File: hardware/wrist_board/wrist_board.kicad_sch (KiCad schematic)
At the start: 0 parts

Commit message: Added hierarchical pages and 3v3 circuitry
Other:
- added sheet ESP and Comms (esp_and_comms.kicad_sch)
- added sheet power (power.kicad_sch)
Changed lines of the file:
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@@
 	(generator_version "9.0")
 	(paper "A4")
+	(sheet
+		(at 64.77 53.34)
+		(size 31.75 25.4)
+		(exclude_from_sim no)
+		(in_bom yes)
+		(on_board yes)
+		(dnp no)
+		(fields_autoplaced yes)
+		(stroke
+			(width 0.1524)
+			(type solid)
+		)
+		(fill
+			(color 0 0 0 0.0000)
+		)
+		(property "Sheetname" "power"
+			(at 64.77 52.6284 0)
+			(effects
+				(font
+					(size 1.27 1.27)
+				)
+				(justify left bottom)
+			)
+		)
+		(property "Sheetfile" "power.kicad_sch"
+			(at 64.77 79.3246 0)
+			(effects
+				(font
+					(size 1.27 1.27)
+				)
+				(justify left top)
+			)
+		)
+		(instances
+			(project "wrist_board"
+				(path "/530b8e3e-eee5-4922-ab86-607fb3fa4192"
+					(page "2")
+				)
+			)
+		)
+	)
+	(sheet
+		(at 101.6 53.34)
+		(size 35.56 25.4)
+		(exclude_from_sim no)
+		(in_bom yes)
+		(on_board yes)
+		(dnp no)
+		(fields_autoplaced yes)
+		(stroke
+			(width 0.1524)
+			(type solid)
+		)
+		(fill
+			(color 0 0 0 0.0000)
+		)
+		(property "Sheetname" "ESP and Comms"
+			(at 101.6 52.6284 0)
+			(effects
+				(font
+					(size 1.27 1.27)
+				)
+				(justify left bottom)
+			)
+		)
+		(property "Sheetfile" "esp_and_comms.kicad_sch"
+			(at 101.6 79.3246 0)
+			(effects
+				(font
+					(size 1.27 1.27)
+				)
+				(justify left top)
+			)
+		)
+		(instances
+			(project "wrist_board"
+				(path "/530b8e3e-eee5-4922-ab86-607fb3fa4192"
+					(page "3")
+				)
+			)
+		)
+	)
 	(sheet_instances
 		(path "/"

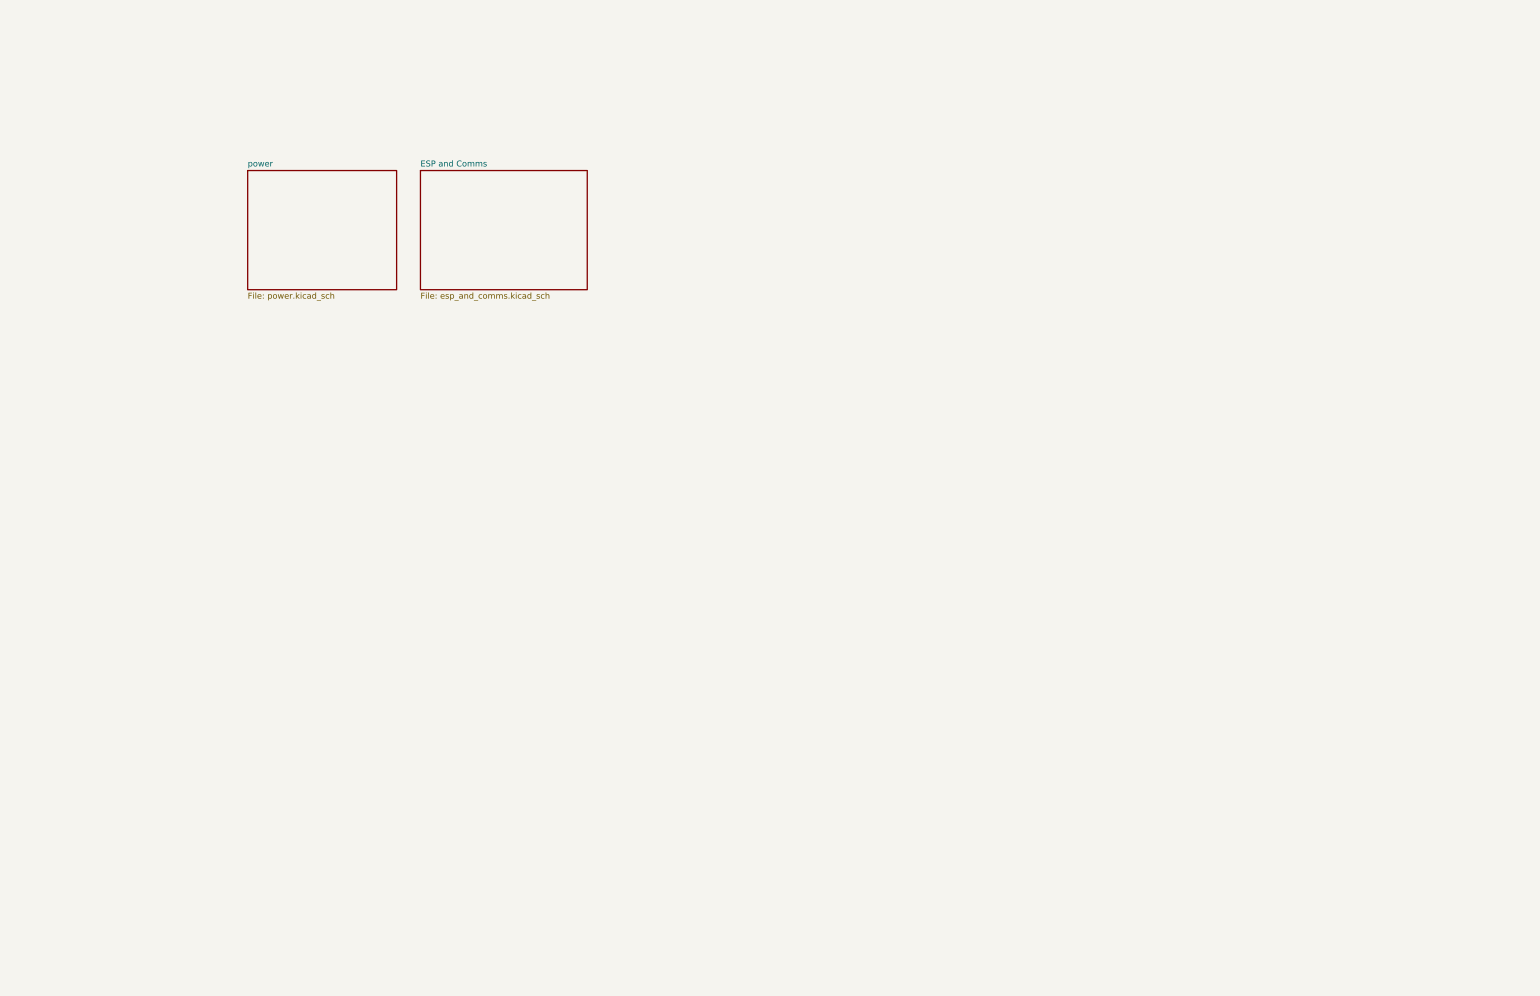
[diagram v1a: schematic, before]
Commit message: Schematics condensed into one, labels added
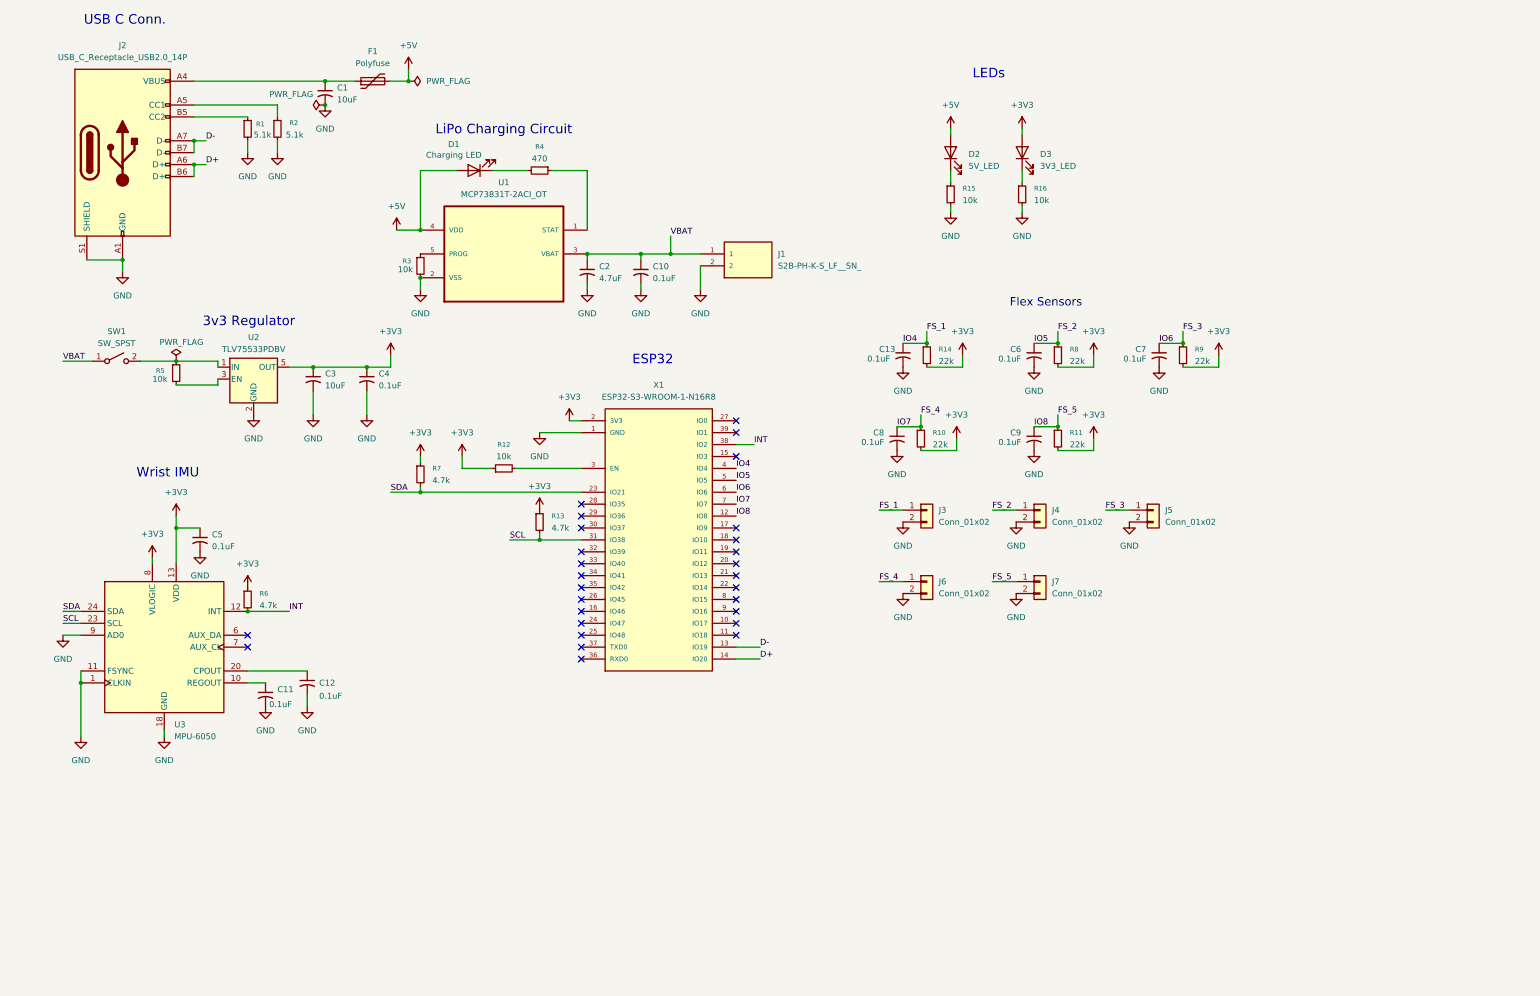
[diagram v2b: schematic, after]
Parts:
- added C1, C3: 10uF, Capacitor_SMD:C_0201_0603Metric, symbol Device:C_Small_US
- added C10, C11, C12, C13, C4, C5, C6, C7, C8, C9: 0.1uF, Capacitor_SMD:C_0402_1005Metric, symbol Device:C_Small_US
- added C2: 4.7uF, Capacitor_SMD:C_0201_0603Metric, symbol Device:C_Small_US
- added D1: Charging LED, LED_SMD:LED_0201_0603Metric, symbol Device:LED
- added D2: 5V_LED, LED_SMD:LED_0201_0603Metric, symbol Device:LED
- added D3: 3V3_LED, LED_SMD:LED_0201_0603Metric, symbol Device:LED
- added F1: Polyfuse, Fuse:Fuse_0805_2012Metric, symbol Device:Polyfuse
- added J1: S2B-PH-K-S_LF__SN_, S2B-PH-K-S_LF__SN_:JST_S2B-PH-K-S_LF__SN_, symbol S2B-PH-K-S_LF__SN_:S2B-PH-K-S_LF__SN_
- added J2: USB_C_Receptacle_USB2.0_14P, Connector_USB:USB_C_Receptacle_GCT_USB4105-xx-A_16P_TopMnt_Horizontal, symbol Connector:USB_C_Receptacle_USB2.0_14P
- added J3, J4, J5, J6, J7: Conn_01x02, Connector_PinHeader_2.54mm:PinHeader_1x02_P2.54mm_Vertical, symbol Connector_Generic:Conn_01x02
- added R1, R2: 5.1k, Resistor_SMD:R_0402_1005Metric, symbol Device:R_Small
- added R10, R11, R14, R8, R9: 22k, Resistor_SMD:R_0402_1005Metric, symbol Device:R_Small
- added R12, R5: 10k, Resistor_SMD:R_0402_1005Metric, symbol Device:R_Small
- added R13, R6, R7: 4.7k, Resistor_SMD:R_0402_1005Metric, symbol Device:R_Small
- added R15, R16: 10k, Resistor_SMD:R_0603_1608Metric, symbol Device:R_Small
- added R3: 10k, LED_SMD:LED_0402_1005Metric, symbol Device:R_Small
- added R4: 470, Resistor_SMD:R_0603_1608Metric, symbol Device:R_Small
- added SW1: SW_SPST, Button_Switch_THT:SW_DIP_SPSTx01_Slide_6.7x4.1mm_W7.62mm_P2.54mm_LowProfile, symbol Switch:SW_SPST
- added U1: MCP73831T-2ACI_OT, MCP73831T-2ACI_OT:SOT95P280X145-5N, symbol MCP73831T-2ACI_OT:MCP73831T-2ACI_OT
- added U2: TLV75533PDBV, Package_TO_SOT_SMD:SOT-23-5, symbol Regulator_Linear:TLV75533PDBV
- added U3: MPU-6050, Sensor_Motion:InvenSense_QFN-24_4x4mm_P0.5mm, symbol Sensor_Motion:MPU-6050
- added X1: ESP32-S3-WROOM-1-N16R8, ESP32-S3-WROOM-1-N16R8:ESP32S3WROOM1N8R2, symbol ESP32-S3-WROOM-1-N16R8:ESP32-S3-WROOM-1-N16R8
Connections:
- new net: D3.1 (K), R16.1
- new net: D1.1 (K), R4.2
- new net: C10.1, C2.1, J1.1, SW1.1 (A), U1.3 (VBAT)
- new net: R12.2, X1.3 (EN)
- new net: C1.1, F1.1, J2.A4 (VBUS), J2.A9 (VBUS), J2.B4 (VBUS), J2.B9 (VBUS)
- new net: C11.1, U3.10 (REGOUT)
- new net: C12.1, U3.20 (CPOUT)
- new net: D2.1 (K), R15.1
- new net: R5.1, SW1.2 (B), U2.1 (IN)
- new net: R4.1, U1.1 (STAT)
- new net: R3.1, U1.5 (PROG)
- new net: J2.B5 (CC2), R1.1
- new net: J2.A5 (CC1), R2.1
- new net: R5.2, U2.3 (EN)
- new net +3V3: C3.1, C4.1, C5.1, D3.2 (A), R10.2, R11.2, R12.1, R13.1, R14.2, R6.1, R7.1, R8.2, R9.2, U2.5 (OUT), U3.13 (VDD), U3.8 (VLOGIC), X1.2 (3V3)
- new net +5V: D1.2 (A), D2.2 (A), F1.2, U1.4 (VDD)
- new net D+: J2.A6 (D+), J2.B6 (D+), X1.14 (IO20)
- new net D-: J2.A7 (D-), J2.B7 (D-), X1.13 (IO19)
- new net FS_1: C13.1, J3.1 (Pin_1), R14.1, X1.4 (IO4)
- new net FS_2: C6.1, J4.1 (Pin_1), R8.1, X1.5 (IO5)
- new net FS_3: C7.1, J5.1 (Pin_1), R9.1, X1.6 (IO6)
- new net FS_4: C8.1, J6.1 (Pin_1), R10.1, X1.7 (IO7)
- new net FS_5: C9.1, J7.1 (Pin_1), R11.1, X1.12 (IO8)
- new net GND: C1.2, C10.2, C11.2, C12.2, C13.2, C2.2, C3.2, C4.2, C5.2, C6.2, C7.2, C8.2, C9.2, J1.2, J2.A1 (GND), J2.A12 (GND), J2.B1 (GND), J2.B12 (GND), J2.S1 (SHIELD), J3.2 (Pin_2), J4.2 (Pin_2), J5.2 (Pin_2), J6.2 (Pin_2), J7.2 (Pin_2), R1.2, R15.2, R16.2, R2.2, R3.2, U1.2 (VSS), U2.2 (GND), U3.1 (CLKIN), U3.11 (FSYNC), U3.18 (GND), U3.9 (AD0), X1.1 (GND), X1.40 (GND), X1.41 (GND), X1.42 (GND), X1.43 (GND), X1.44 (GND), X1.45 (GND), X1.46 (GND), X1.47 (GND), X1.48 (GND), X1.49 (GND)
- new net INT: R6.2, U3.12 (INT), X1.38 (IO2)
- new net SCL: R13.2, U3.23 (SCL), X1.31 (IO38)
- new net SDA: R7.2, U3.24 (SDA), X1.23 (IO21)
- no-connect marks 0 -> 28
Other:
- removed sheet ESP and Comms
- removed sheet power
- note added: "3v3 Regulator"
- note added: "ESP32"
- note added: "Flex Sensors"
- note added: "LEDs"
- note added: "LiPo Charging Circuit"
- note added: "USB C Conn."
- note added: "Wrist IMU"

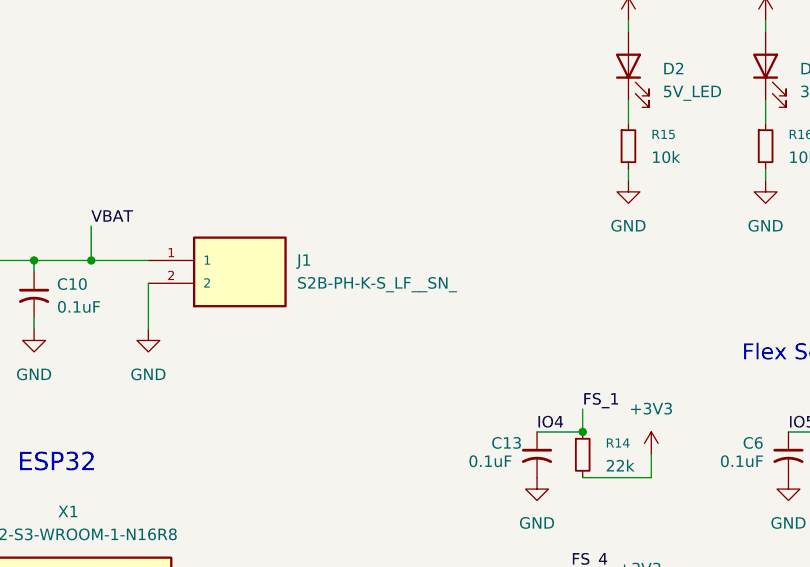
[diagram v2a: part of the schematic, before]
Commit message: New board orientation + USB/PWR routing
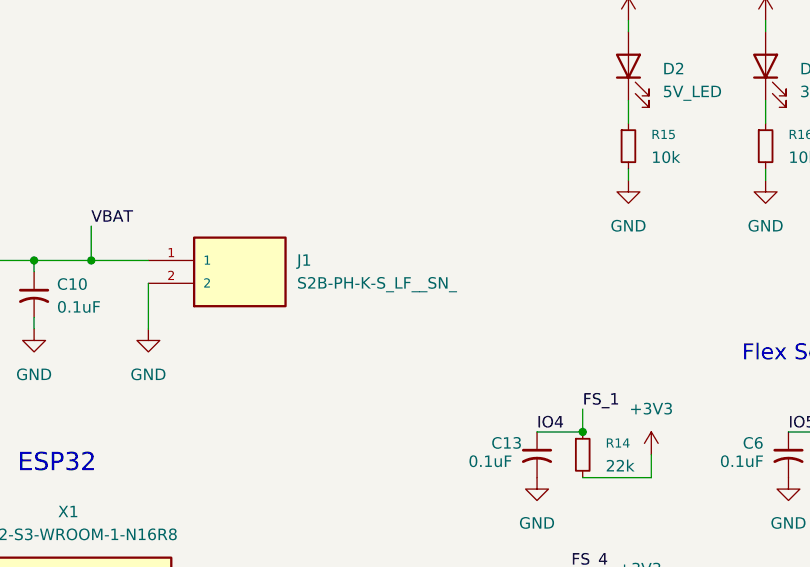
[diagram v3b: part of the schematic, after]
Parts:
- C1, C2, C3: footprint Capacitor_SMD:C_0201_0603Metric -> Capacitor_SMD:C_0805_2012Metric
- C10, C11, C12, C13, C4, C5, C6, C7, C8, C9: footprint Capacitor_SMD:C_0402_1005Metric -> Capacitor_SMD:C_0805_2012Metric
- D1, D2, D3: footprint LED_SMD:LED_0201_0603Metric -> LED_SMD:LED_0805_2012Metric
- R1, R10, R11, R12, R13, R14, R2, R5, R6, R7, R8, R9: footprint Resistor_SMD:R_0402_1005Metric -> Resistor_SMD:R_0805_2012Metric
- R15, R16, R4: footprint Resistor_SMD:R_0603_1608Metric -> Resistor_SMD:R_0805_2012Metric
- R3: footprint LED_SMD:LED_0402_1005Metric -> Resistor_SMD:R_0805_2012Metric
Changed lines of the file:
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@@
 			)
 		)
-		(property "Footprint" "Capacitor_SMD:C_0402_1005Metric"
+		(property "Footprint" "Capacitor_SMD:C_0805_2012Metric"
 			(at 204.47 92.71 0)
 			(effects
@@
 			)
 		)
-		(property "Footprint" "Resistor_SMD:R_0603_1608Metric"
+		(property "Footprint" "Resistor_SMD:R_0805_2012Metric"
 			(at 229.87 58.42 0)
 			(effects
@@
 			)
 		)
-		(property "Footprint" "LED_SMD:LED_0201_0603Metric"
+		(property "Footprint" "LED_SMD:LED_0805_2012Metric"
 			(at 113.03 53.34 0)
 			(effects
@@
 		(on_board yes)
 		(dnp no)
-		(fields_autoplaced yes)
 		(property "Reference" "J1"
 			(at 177.8 71.1199 0)
@@
 		)
 		(property "Value" "S2B-PH-K-S_LF__SN_"
-			(at 177.8 73.6599 0)
+			(at 177.8 73.66 0)
 			(effects
 				(font
@@
 			)
 		)
-		(property "Footprint" "Resistor_SMD:R_0603_1608Metric"
+		(property "Footprint" "Resistor_SMD:R_0805_2012Metric"
 			(at 214.63 58.42 0)
 			(effects
@@
 			)
 		)
-		(property "Footprint" "Resistor_SMD:R_0402_1005Metric"
+		(property "Footprint" "Resistor_SMD:R_0805_2012Metric"
 			(at 264.16 92.71 0)
 			(effects
@@
 			)
 		)
-		(property "Footprint" "Capacitor_SMD:C_0402_1005Metric"
+		(property "Footprint" "Capacitor_SMD:C_0805_2012Metric"
 			(at 148.59 74.93 0)
 			(effects
@@
 			)
 		)
-		(property "Footprint" "Capacitor_SMD:C_0402_1005Metric"
+		(property "Footprint" "Capacitor_SMD:C_0805_2012Metric"
 			(at 232.41 92.71 0)
 			(effects
@@
 			)
 		)
-		(property "Footprint" "Resistor_SMD:R_0402_1005Metric"
+		(property "Footprint" "Resistor_SMD:R_0805_2012Metric"
 			(at 209.55 92.71 0)
 			(effects
@@
 			)
 		)
-		(property "Footprint" "Resistor_SMD:R_0402_1005Metric"
+		(property "Footprint" "Resistor_SMD:R_0805_2012Metric"
 			(at 64.77 144.78 0)
 			(effects
@@
 			)
 		)
-		(property "Footprint" "Capacitor_SMD:C_0402_1005Metric"
+		(property "Footprint" "Capacitor_SMD:C_0805_2012Metric"
 			(at 77.47 162.56 0)
 			(effects
@@
 			)
 		)
-		(property "Footprint" "Resistor_SMD:R_0402_1005Metric"
+		(property "Footprint" "Resistor_SMD:R_0805_2012Metric"
 			(at 119.38 116.84 0)
 			(effects
@@
 			)
 		)
-		(property "Footprint" "Capacitor_SMD:C_0201_0603Metric"
+		(property "Footprint" "Capacitor_SMD:C_0805_2012Metric"
 			(at 78.74 97.79 0)
 			(effects
@@
 			)
 		)
-		(property "Footprint" "Resistor_SMD:R_0402_1005Metric"
+		(property "Footprint" "Resistor_SMD:R_0805_2012Metric"
 			(at 237.49 92.71 0)
 			(effects
@@
 			)
 		)
-		(property "Footprint" "LED_SMD:LED_0402_1005Metric"
+		(property "Footprint" "Resistor_SMD:R_0805_2012Metric"
 			(at 101.6 73.66 0)
 			(effects
@@
 			)
 		)
-		(property "Footprint" "Resistor_SMD:R_0402_1005Metric"
+		(property "Footprint" "Resistor_SMD:R_0805_2012Metric"
 			(at 64.77 44.45 0)
 			(effects
@@
 			)
 		)
-		(property "Footprint" "Capacitor_SMD:C_0402_1005Metric"
+		(property "Footprint" "Capacitor_SMD:C_0805_2012Metric"
 			(at 203.2 110.49 0)
 			(effects
@@
 			)
 		)
-		(property "Footprint" "Capacitor_SMD:C_0402_1005Metric"
+		(property "Footprint" "Capacitor_SMD:C_0805_2012Metric"
 			(at 232.41 110.49 0)
 			(effects
@@
 			)
 		)
-		(property "Footprint" "Resistor_SMD:R_0402_1005Metric"
+		(property "Footprint" "Resistor_SMD:R_0805_2012Metric"
 			(at 101.6 118.11 0)
 			(effects
@@
 			)
 		)
-		(property "Footprint" "LED_SMD:LED_0201_0603Metric"
+		(property "Footprint" "LED_SMD:LED_0805_2012Metric"
 			(at 229.87 49.53 0)
 			(effects
@@
 			)
 		)
-		(property "Footprint" "Capacitor_SMD:C_0402_1005Metric"
+		(property "Footprint" "Capacitor_SMD:C_0805_2012Metric"
 			(at 259.08 92.71 0)
 			(effects
@@
 			)
 		)
-		(property "Footprint" "Resistor_SMD:R_0402_1005Metric"
+		(property "Footprint" "Resistor_SMD:R_0805_2012Metric"
 			(at 49.53 96.52 0)
 			(effects
@@
 			)
 		)
-		(property "Footprint" "Capacitor_SMD:C_0402_1005Metric"
+		(property "Footprint" "Capacitor_SMD:C_0805_2012Metric"
 			(at 90.17 97.79 0)
 			(effects
@@
 			)
 		)
-		(property "Footprint" "Capacitor_SMD:C_0201_0603Metric"
+		(property "Footprint" "Capacitor_SMD:C_0805_2012Metric"
 			(at 137.16 74.93 0)
 			(effects
@@
 			)
 		)
-		(property "Footprint" "Resistor_SMD:R_0603_1608Metric"
+		(property "Footprint" "Resistor_SMD:R_0805_2012Metric"
 			(at 127 53.34 0)
 			(effects
@@
 			)
 		)
-		(property "Footprint" "Capacitor_SMD:C_0201_0603Metric"
+		(property "Footprint" "Capacitor_SMD:C_0805_2012Metric"
 			(at 81.28 36.83 0)
 			(effects
@@
 			)
 		)
-		(property "Footprint" "Resistor_SMD:R_0402_1005Metric"
+		(property "Footprint" "Resistor_SMD:R_0805_2012Metric"
 			(at 127 128.27 0)
 			(effects
@@
 			)
 		)
-		(property "Footprint" "Capacitor_SMD:C_0402_1005Metric"
+		(property "Footprint" "Capacitor_SMD:C_0805_2012Metric"
 			(at 54.61 132.08 0)
 			(effects
@@
 			)
 		)
-		(property "Footprint" "LED_SMD:LED_0201_0603Metric"
+		(property "Footprint" "LED_SMD:LED_0805_2012Metric"
 			(at 214.63 49.53 0)
 			(effects
@@
 			)
 		)
-		(property "Footprint" "Capacitor_SMD:C_0402_1005Metric"
+		(property "Footprint" "Capacitor_SMD:C_0805_2012Metric"
 			(at 68.58 165.1 0)
 			(effects
@@
 			)
 		)
-		(property "Footprint" "Resistor_SMD:R_0402_1005Metric"
+		(property "Footprint" "Resistor_SMD:R_0805_2012Metric"
 			(at 237.49 110.49 0)
 			(effects
@@
 			)
 		)
-		(property "Footprint" "Resistor_SMD:R_0402_1005Metric"
+		(property "Footprint" "Resistor_SMD:R_0805_2012Metric"
 			(at 71.12 44.45 0)
 			(effects
@@
 			)
 		)
-		(property "Footprint" "Resistor_SMD:R_0402_1005Metric"
+		(property "Footprint" "Resistor_SMD:R_0805_2012Metric"
 			(at 208.28 110.49 0)
 			(effects
